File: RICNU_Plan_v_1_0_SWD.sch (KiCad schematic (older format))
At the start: 8 parts, among them J7 FH19C-6S-0.5SH(05)

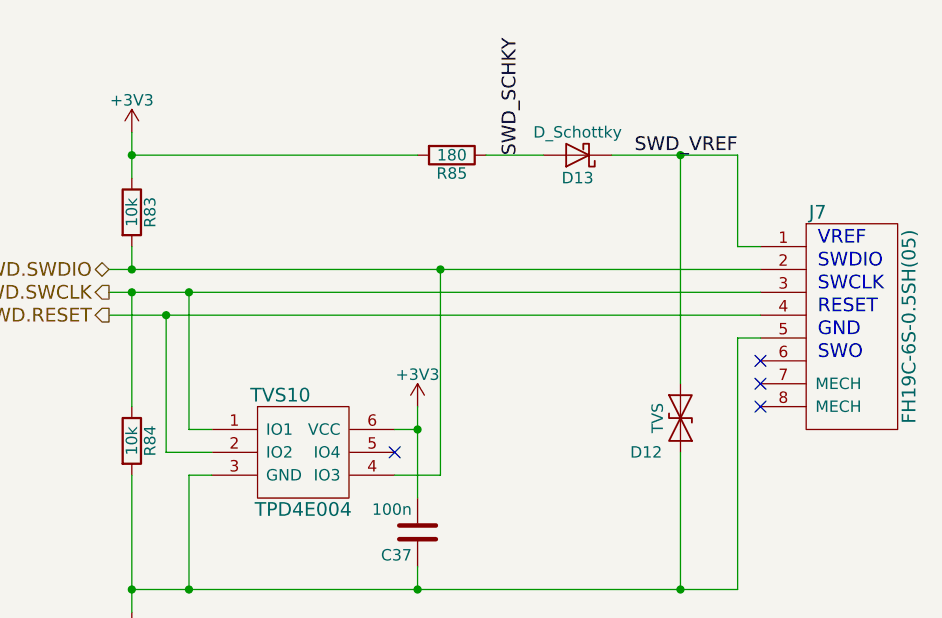
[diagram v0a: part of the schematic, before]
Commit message: Re-routed CAN, RS-485, and debug connectors (wrong polarity in all)
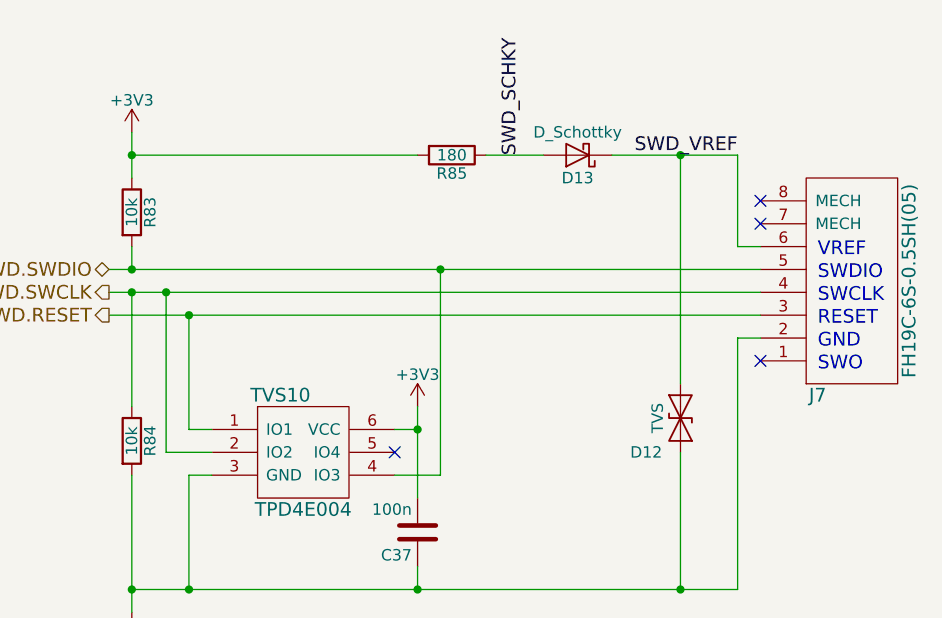
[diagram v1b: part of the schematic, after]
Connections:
- net GND: now also J7.2; no longer J7.5
- net SWD.RESET: now also J7.3, TVS10.1 (IO1); no longer J7.4, TVS10.2 (IO2)
- net SWD.SWCLK: now also J7.4, TVS10.2 (IO2); no longer J7.3, TVS10.1 (IO1)
- net SWD.SWDIO: now also J7.5; no longer J7.2
- net SWD_VREF: now also J7.6; no longer J7.1
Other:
- moved on the sheet: J7
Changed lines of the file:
@@
 $EndComp
 $Comp
-L GND #PWR081
+L GND #PWR082
 U 1 1 59FB58C0
 P 4600 5100
-F 0 "#PWR081" H 4600 4850 50  0001 C CNN
+F 0 "#PWR082" H 4600 4850 50  0001 C CNN
 F 1 "GND" H 4600 4950 50  0000 C CNN
 F 2 "" H 4600 5100 50  0001 C CNN
@@
 CPDQC3V3T-HF
 $Comp
-L +3V3 #PWR082
+L +3V3 #PWR083
 U 1 1 59FB58D0
 P 5850 4200
-F 0 "#PWR082" H 5850 4050 50  0001 C CNN
+F 0 "#PWR083" H 5850 4050 50  0001 C CNN
 F 1 "+3V3" H 5850 4340 50  0000 C CNN
 F 2 "" H 5850 4200 50  0001 C CNN
@@
 NoConn ~ 7350 4000
 $Comp
-L +3V3 #PWR083
+L +3V3 #PWR084
 U 1 1 59FA4044
 P 4600 3000
-F 0 "#PWR083" H 4600 2850 50  0001 C CNN
+F 0 "#PWR084" H 4600 2850 50  0001 C CNN
 F 1 "+3V3" H 4600 3140 50  0000 C CNN
 F 2 "" H 4600 3000 50  0001 C CNN
@@
 Wire Wire Line
 	4950 4300 4850 4300
-Wire Wire Line
-	4850 4300 4850 3700
-Connection ~ 4850 3700
+Connection ~ 4750 3700
 Wire Wire Line
 	5750 4300 5850 4300
@@
 	4600 4500 4600 5100
 Connection ~ 4600 5000
-Text Notes 7600 3500 0    60   ~ 0
+Text Notes 7600 3550 0    60   ~ 0
 VREF
-Text Notes 7600 3600 0    60   ~ 0
+Text Notes 7600 3650 0    60   ~ 0
 SWDIO
-Text Notes 7600 3700 0    60   ~ 0
+Text Notes 7600 3750 0    60   ~ 0
 SWCLK
-Text Notes 7600 3800 0    60   ~ 0
+Text Notes 7600 3850 0    60   ~ 0
 RESET
-Text Notes 7600 3900 0    60   ~ 0
+Text Notes 7600 3950 0    60   ~ 0
 GND
-Text Notes 7600 4000 0    60   ~ 0
+Text Notes 7600 4050 0    60   ~ 0
 SWO
 $Comp
 L FH19C-6S-0.5SH(05) J7
 U 1 1 59FA08B1
-P 7750 3850
-F 0 "J7" H 7600 4350 60  0000 C CNN
-F 1 "FH19C-6S-0.5SH(05)" V 8000 3850 60  0000 C CNN
-F 2 "RICNU_Plan_v_1_0:FH19C-6S-0.5SH(05)" H 7700 4050 60  0001 C CNN
-F 3 "" H 7700 4050 60  0001 C CNN
-	1    7750 3850
-	1    0    0    -1
+P 7750 3650
+F 0 "J7" H 7600 4150 60  0000 C CNN
+F 1 "FH19C-6S-0.5SH(05)" V 8000 3650 60  0000 C CNN
+F 2 "RICNU_Plan_v_1_0:FH19C-6S-0.5SH(05)" H 7700 3850 60  0001 C CNN
+F 3 "" H 7700 3850 60  0001 C CNN
+	1    7750 3650
+	1    0    0    1
 $EndComp
 Text Label 7250 3100 2    60   ~ 0
@@
 Text Label 6300 3100 1    60   ~ 0
 SWD_SCHKY
-NoConn ~ 7350 4100
-NoConn ~ 7350 4200
-Wire Wire Line
-	4750 4400 4750 3800
-Connection ~ 4750 3800
+NoConn ~ 7350 3400
+NoConn ~ 7350 3300
+Connection ~ 4850 3800
 Wire Wire Line
 	5950 3600 5950 4500
@@
 	5950 4500 5750 4500
 NoConn ~ 5750 4400
+Wire Wire Line
+	4750 4400 4750 3700
+Wire Wire Line
+	4850 4300 4850 3800
 $EndSCHEMATC

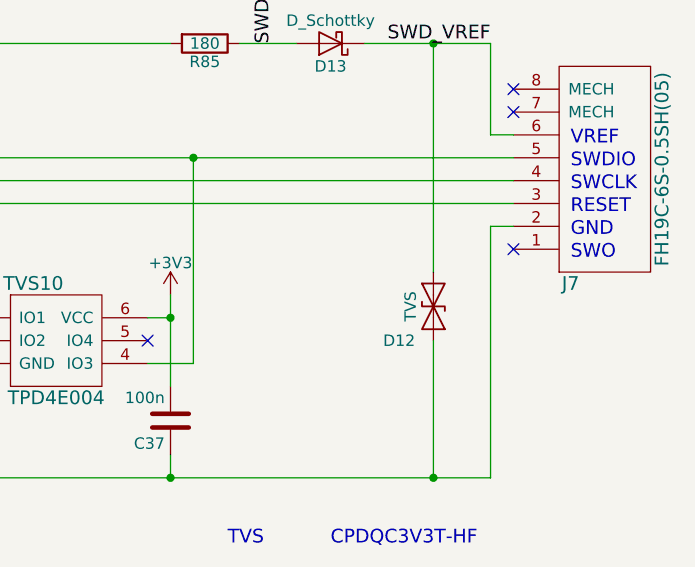
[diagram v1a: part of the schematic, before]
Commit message: Added connections to monitor power, changed CANSTB MCU pin, moved LED pins around
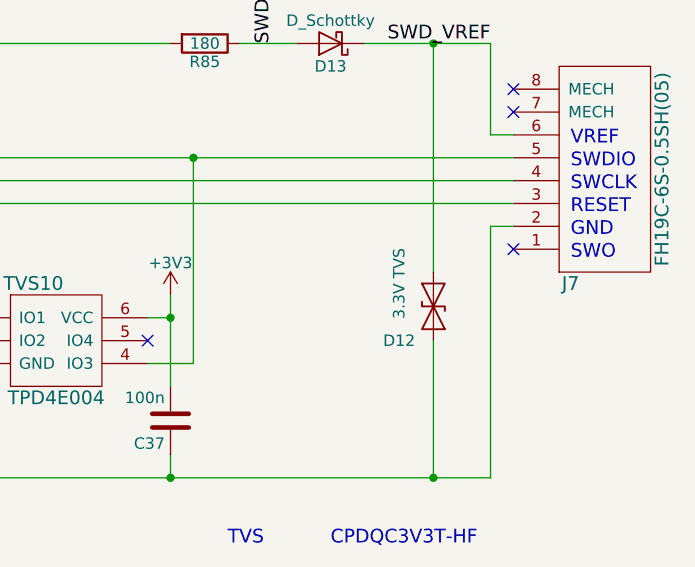
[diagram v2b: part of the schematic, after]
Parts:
- D12: value TVS -> 3.3V TVS
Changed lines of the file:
@@
 P 7000 4250
 F 0 "D12" V 7150 4100 50  0000 C CNN
-F 1 "TVS" H 7000 4150 50  0000 C CNN
+F 1 "3.3V TVS" H 6900 4100 50  0000 C CNN
 F 2 "Diodes_SMD:D_SOD-523" H 7000 4250 50  0001 C CNN
 F 3 "" H 7000 4250 50  0001 C CNN
@@
 $EndComp
 $Comp
-L GND #PWR082
+L GND #PWR083
 U 1 1 59FB58C0
 P 4600 5100
-F 0 "#PWR082" H 4600 4850 50  0001 C CNN
+F 0 "#PWR083" H 4600 4850 50  0001 C CNN
 F 1 "GND" H 4600 4950 50  0000 C CNN
 F 2 "" H 4600 5100 50  0001 C CNN
@@
 CPDQC3V3T-HF
 $Comp
-L +3V3 #PWR083
+L +3V3 #PWR084
 U 1 1 59FB58D0
 P 5850 4200
-F 0 "#PWR083" H 5850 4050 50  0001 C CNN
+F 0 "#PWR084" H 5850 4050 50  0001 C CNN
 F 1 "+3V3" H 5850 4340 50  0000 C CNN
 F 2 "" H 5850 4200 50  0001 C CNN
@@
 NoConn ~ 7350 4000
 $Comp
-L +3V3 #PWR084
+L +3V3 #PWR085
 U 1 1 59FA4044
 P 4600 3000
-F 0 "#PWR084" H 4600 2850 50  0001 C CNN
+F 0 "#PWR085" H 4600 2850 50  0001 C CNN
 F 1 "+3V3" H 4600 3140 50  0000 C CNN
 F 2 "" H 4600 3000 50  0001 C CNN

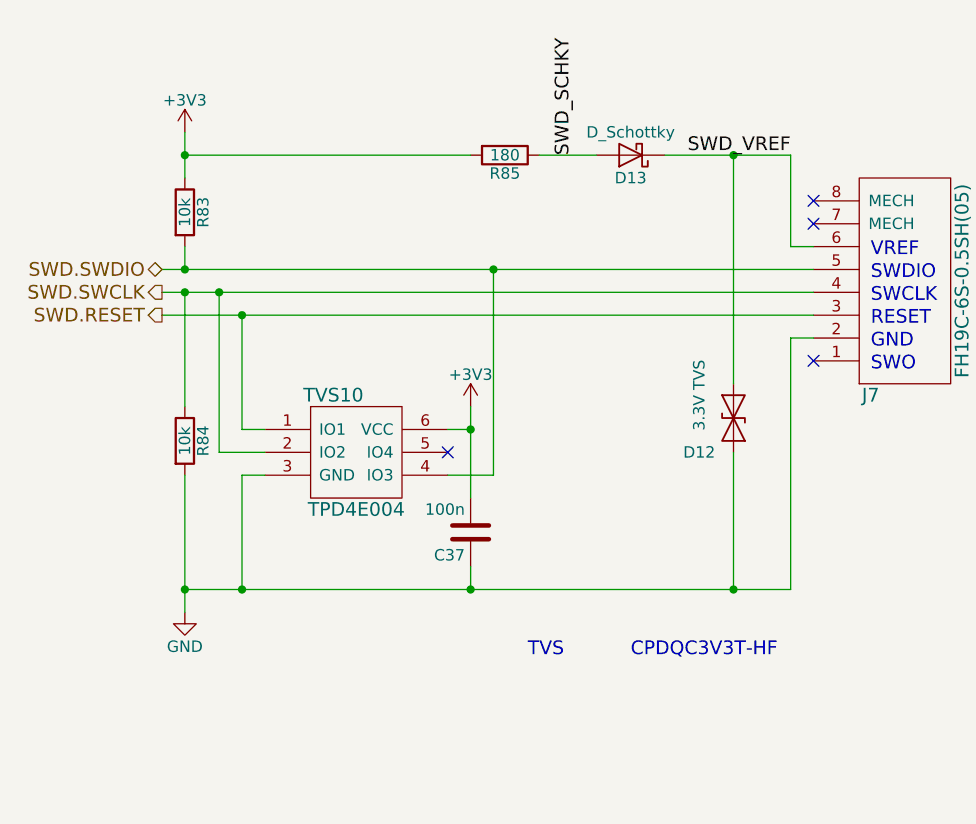
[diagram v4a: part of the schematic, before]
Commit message: Various small changes like comment removal
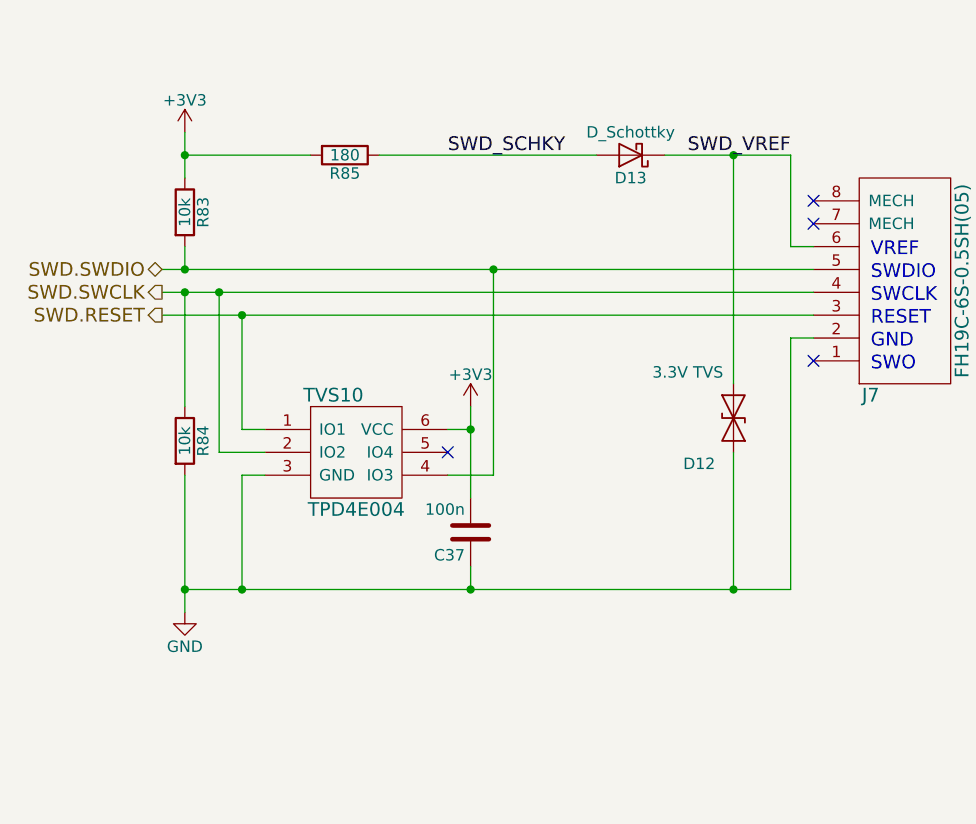
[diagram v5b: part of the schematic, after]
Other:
- note removed: "CPDQC3V3T-HF"
- note removed: "TVS"
- moved on the sheet: R85
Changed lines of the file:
@@
 U 1 1 59FB58B9
 P 7000 4250
-F 0 "D12" V 7150 4100 50  0000 C CNN
-F 1 "3.3V TVS" H 6900 4100 50  0000 C CNN
+F 0 "D12" V 7200 4100 50  0000 C CNN
+F 1 "3.3V TVS" V 6800 4050 50  0000 C CNN
 F 2 "Diodes_SMD:D_SOD-523" H 7000 4250 50  0001 C CNN
 F 3 "" H 7000 4250 50  0001 C CNN
@@
 	1    0    0    -1
 $EndComp
-Text Notes 6550 5300 0    60   ~ 0
-CPDQC3V3T-HF
 $Comp
 L +3V3 #PWR089
@@
 Text Notes 800  7250 0    60   ~ 0
 *  Zener not necessary? I am supplying the 3V3 to the debugger for level translation; overvoltage not likely\n
-Text Notes 6100 5300 0    60   ~ 0
-TVS
-$Comp
-L R R85
-U 1 1 59FB5908
-P 6000 3100
-F 0 "R85" V 6080 3100 50  0000 C CNN
-F 1 "180" V 6000 3100 50  0000 C CNN
-F 2 "Resistors_SMD:R_0402_NoSilk" V 5930 3100 50  0001 C CNN
-F 3 "" H 6000 3100 50  0001 C CNN
-	1    6000 3100
-	0    1    1    0
-$EndComp
 $Comp
 L D_Schottky D13
@@
 $EndComp
 Wire Wire Line
-	4500 3600 7350 3600
-Wire Wire Line
-	4500 3700 7350 3700
+	4500 3600 4600 3600
+Wire Wire Line
+	4600 3600 5950 3600
+Wire Wire Line
+	5950 3600 7350 3600
+Wire Wire Line
+	4500 3700 4600 3700
+Wire Wire Line
+	4600 3700 4750 3700
+Wire Wire Line
+	4750 3700 7350 3700
 Wire Wire Line
 	7250 3500 7350 3500
@@
 	7250 3100 7250 3500
 Wire Wire Line
-	6400 3100 6150 3100
-Wire Wire Line
-	4600 5000 7250 5000
+	6400 3100 5450 3100
+Wire Wire Line
+	4600 5000 4850 5000
+Wire Wire Line
+	4850 5000 5850 5000
+Wire Wire Line
+	5850 5000 7000 5000
+Wire Wire Line
+	7000 5000 7250 5000
 Wire Wire Line
 	7250 5000 7250 3900
@@
 	5750 4300 5850 4300
 Wire Wire Line
-	5850 4200 5850 4600
+	5850 4200 5850 4300
+Wire Wire Line
+	5850 4300 5850 4600
 Connection ~ 5850 4300
 Wire Wire Line
@@
 Connection ~ 5850 5000
 Wire Wire Line
-	4500 3800 7350 3800
+	4500 3800 4850 3800
+Wire Wire Line
+	4850 3800 7350 3800
 Connection ~ 4850 5000
 Wire Wire Line
@@
 Connection ~ 4600 3600
 Wire Wire Line
-	4600 3000 4600 3200
-Wire Wire Line
-	4600 3100 5850 3100
-Wire Wire Line
-	6700 3100 7250 3100
+	4600 3000 4600 3100
+Wire Wire Line
+	4600 3100 4600 3200
+Wire Wire Line
+	4600 3100 5150 3100
+Wire Wire Line
+	6700 3100 7000 3100
+Wire Wire Line
+	7000 3100 7250 3100
 Connection ~ 4600 3100
 Wire Wire Line
 	4850 4500 4850 5000
 Wire Wire Line
-	4600 4500 4600 5100
+	4600 4500 4600 5000
+Wire Wire Line
+	4600 5000 4600 5100
 Connection ~ 4600 5000
 Text Notes 7600 3550 0    60   ~ 0
@@
 Text Label 7250 3100 2    60   ~ 0
 SWD_VREF
-Text Label 6300 3100 1    60   ~ 0
+Text Label 5750 3100 0    60   ~ 0
 SWD_SCHKY
 NoConn ~ 7350 3400
@@
 Wire Wire Line
 	4850 4300 4850 3800
+$Comp
+L R R85
+U 1 1 59FB5908
+P 5300 3100
+F 0 "R85" V 5380 3100 50  0000 C CNN
+F 1 "180" V 5300 3100 50  0000 C CNN
+F 2 "Resistors_SMD:R_0402_NoSilk" V 5230 3100 50  0001 C CNN
+F 3 "" H 5300 3100 50  0001 C CNN
+	1    5300 3100
+	0    1    1    0
+$EndComp
 $EndSCHEMATC
